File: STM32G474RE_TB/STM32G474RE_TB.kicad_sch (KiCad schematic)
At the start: 2 parts, among them U1 STM32G474RETx, Y1 ABM8G-24.000MHZ-18-D2Y-T

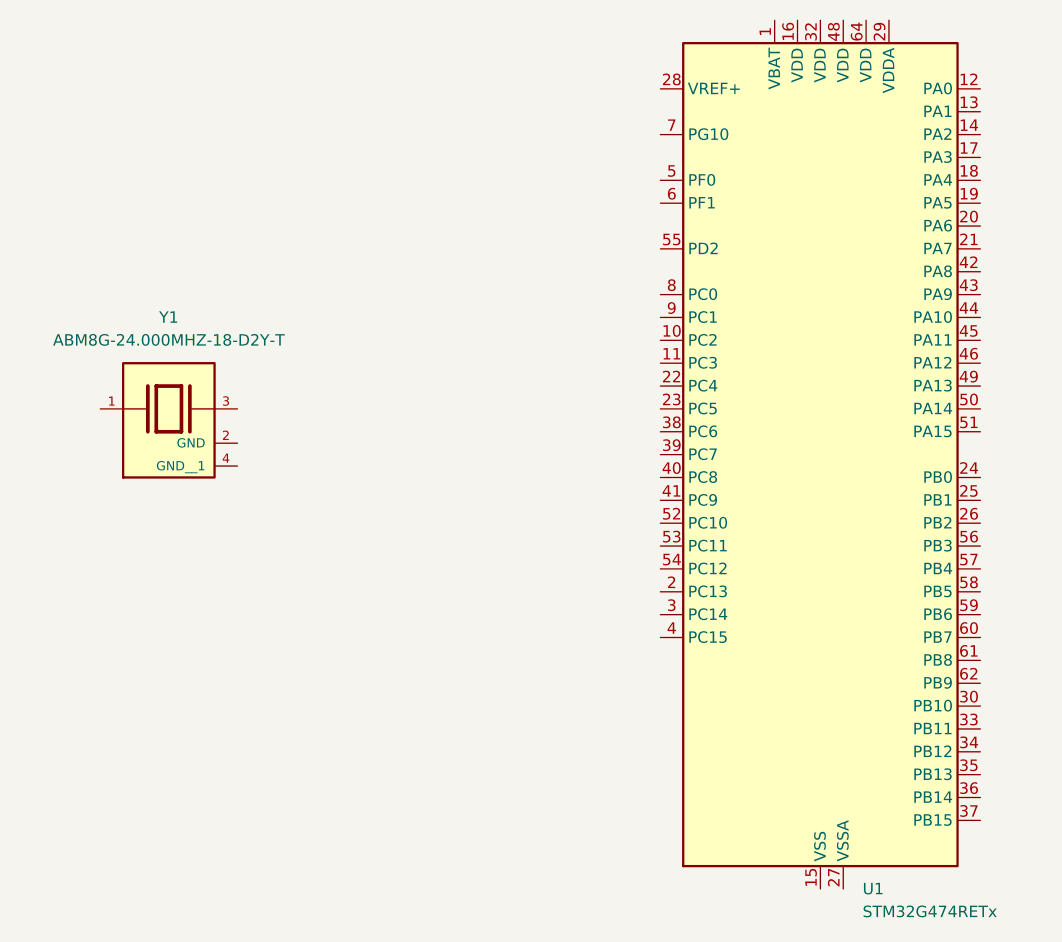
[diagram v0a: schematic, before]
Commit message: Rotated STM32 and adjusted xosc capacitor values.
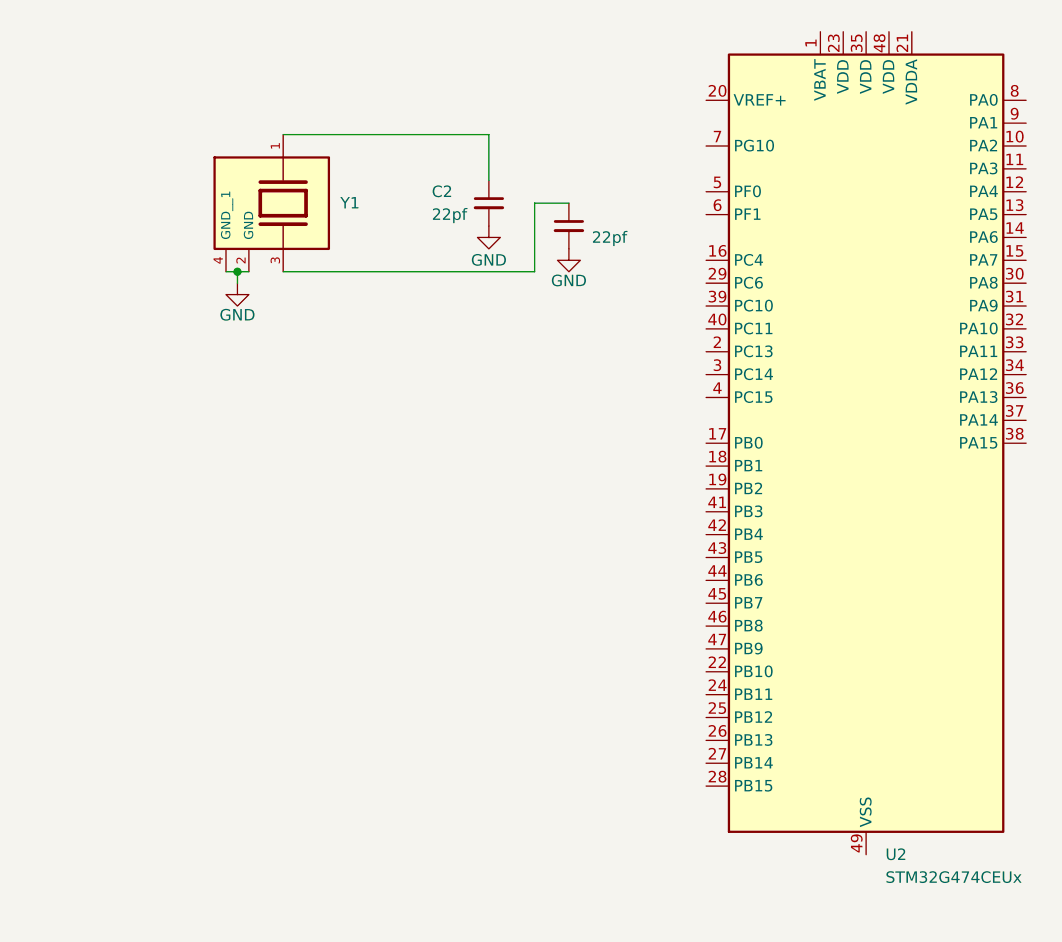
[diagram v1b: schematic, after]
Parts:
- removed U1: STM32G474RETx, Package_QFP:LQFP-64_10x10mm_P0.5mm, symbol MCU_ST_STM32G4:STM32G474RETx
- added C1, C2: 22pf, Capacitor_SMD:C_0603_1608Metric, symbol Device:C_Small
- added U2: STM32G474CEUx, Package_DFN_QFN:QFN-48-1EP_7x7mm_P0.5mm_EP5.6x5.6mm, symbol MCU_ST_STM32G4:STM32G474CEUx
- Y1: footprint ABM8G_24_000MHZ_18_D2Y_T:XTAL_ABM8G-24.000MHZ-18-D2Y-T -> Crystal:Crystal_SMD_Abracon_ABM8G-4Pin_3.2x2.5mm
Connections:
- net at Y1.1: now also C2.1
- net GND: now reaches Y1.2 (GND)
- net GND: now also Y1.4 (GND__1), C1.2, C2.2
- net at Y1.3: now also C1.1
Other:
- moved on the sheet: Y1

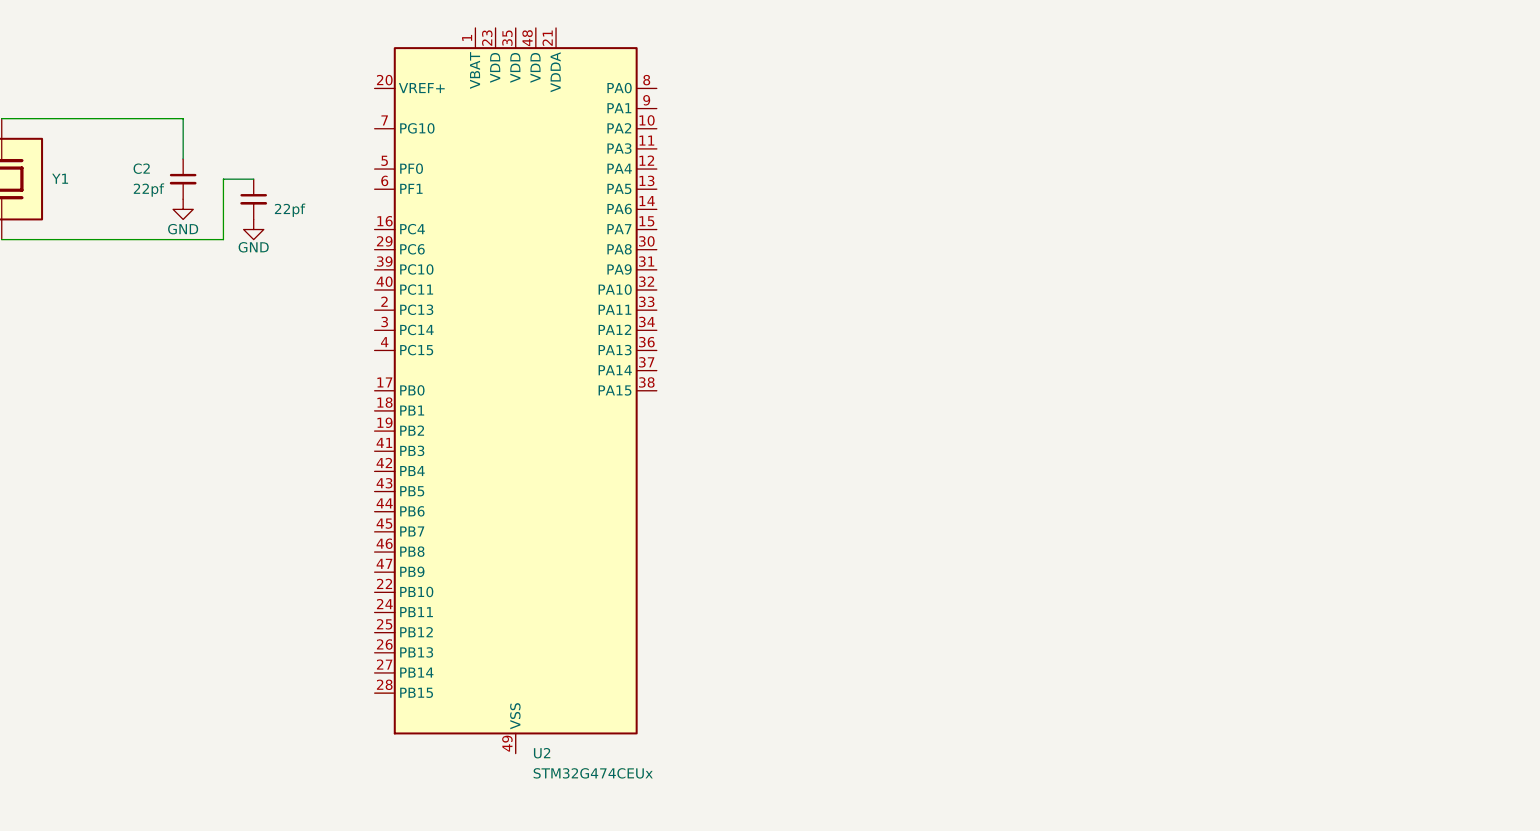
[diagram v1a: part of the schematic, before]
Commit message: Added temporary STM32Cubeide project for pin config.
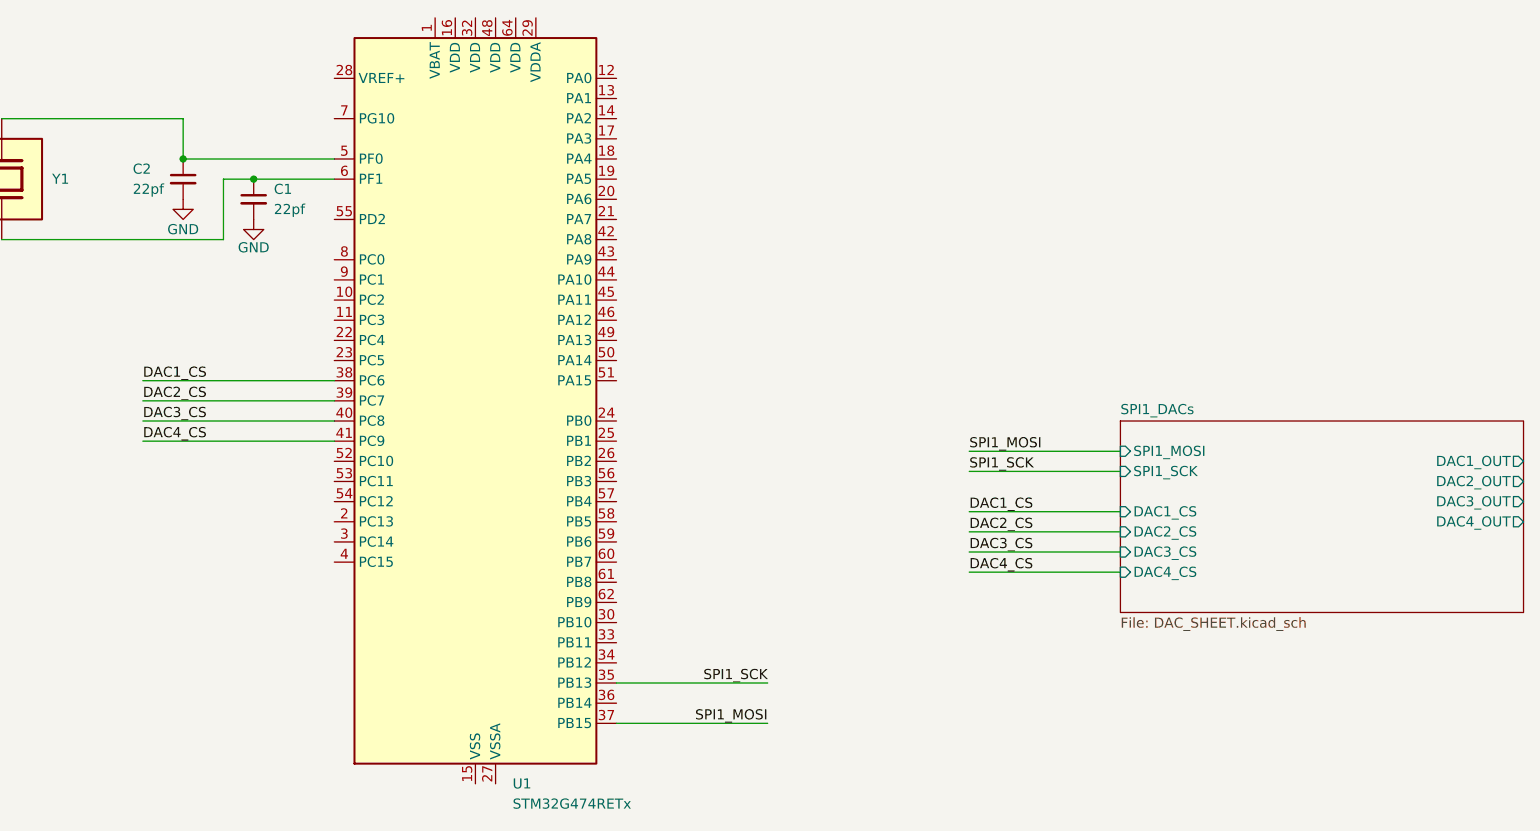
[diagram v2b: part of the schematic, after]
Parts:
- removed U2: STM32G474CEUx, Package_DFN_QFN:QFN-48-1EP_7x7mm_P0.5mm_EP5.6x5.6mm, symbol MCU_ST_STM32G4:STM32G474CEUx
- added U1: STM32G474RETx, Package_QFP:LQFP-64_10x10mm_P0.5mm, symbol MCU_ST_STM32G4:STM32G474RETx
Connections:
- net at C2.1, Y1.1: now also U1.5 (PF0)
- net at C1.1, Y1.3: now also U1.6 (PF1)
- new net: U1.15 (VSS), U1.31 (VSS), U1.47 (VSS), U1.63 (VSS)
- new net DAC1_CS: U1.38 (PC6)
- new net DAC2_CS: U1.39 (PC7)
- new net DAC3_CS: U1.40 (PC8)
- new net DAC4_CS: U1.41 (PC9)
- new net SPI1_MOSI: U1.37 (PB15)
- new net SPI1_SCK: U1.35 (PB13)
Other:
- added sheet SPI1_DACs (DAC_SHEET.kicad_sch)

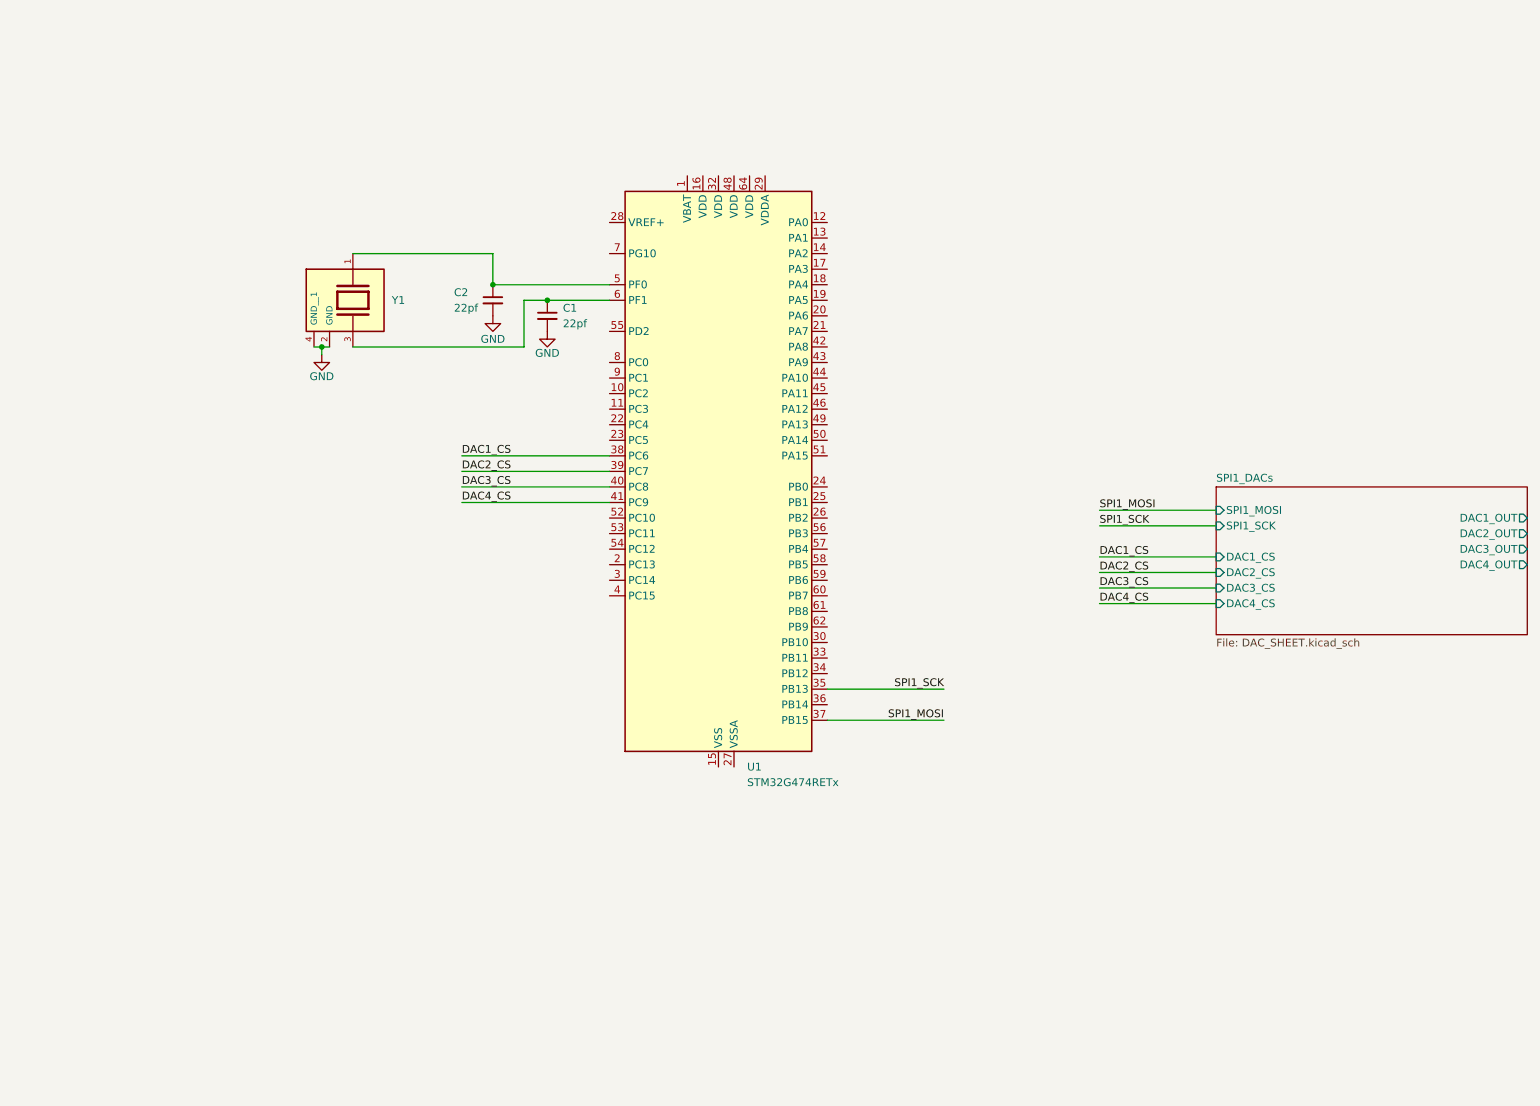
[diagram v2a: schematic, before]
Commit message: Added power LDO and built DAC buffer circuits Added pin descriptions
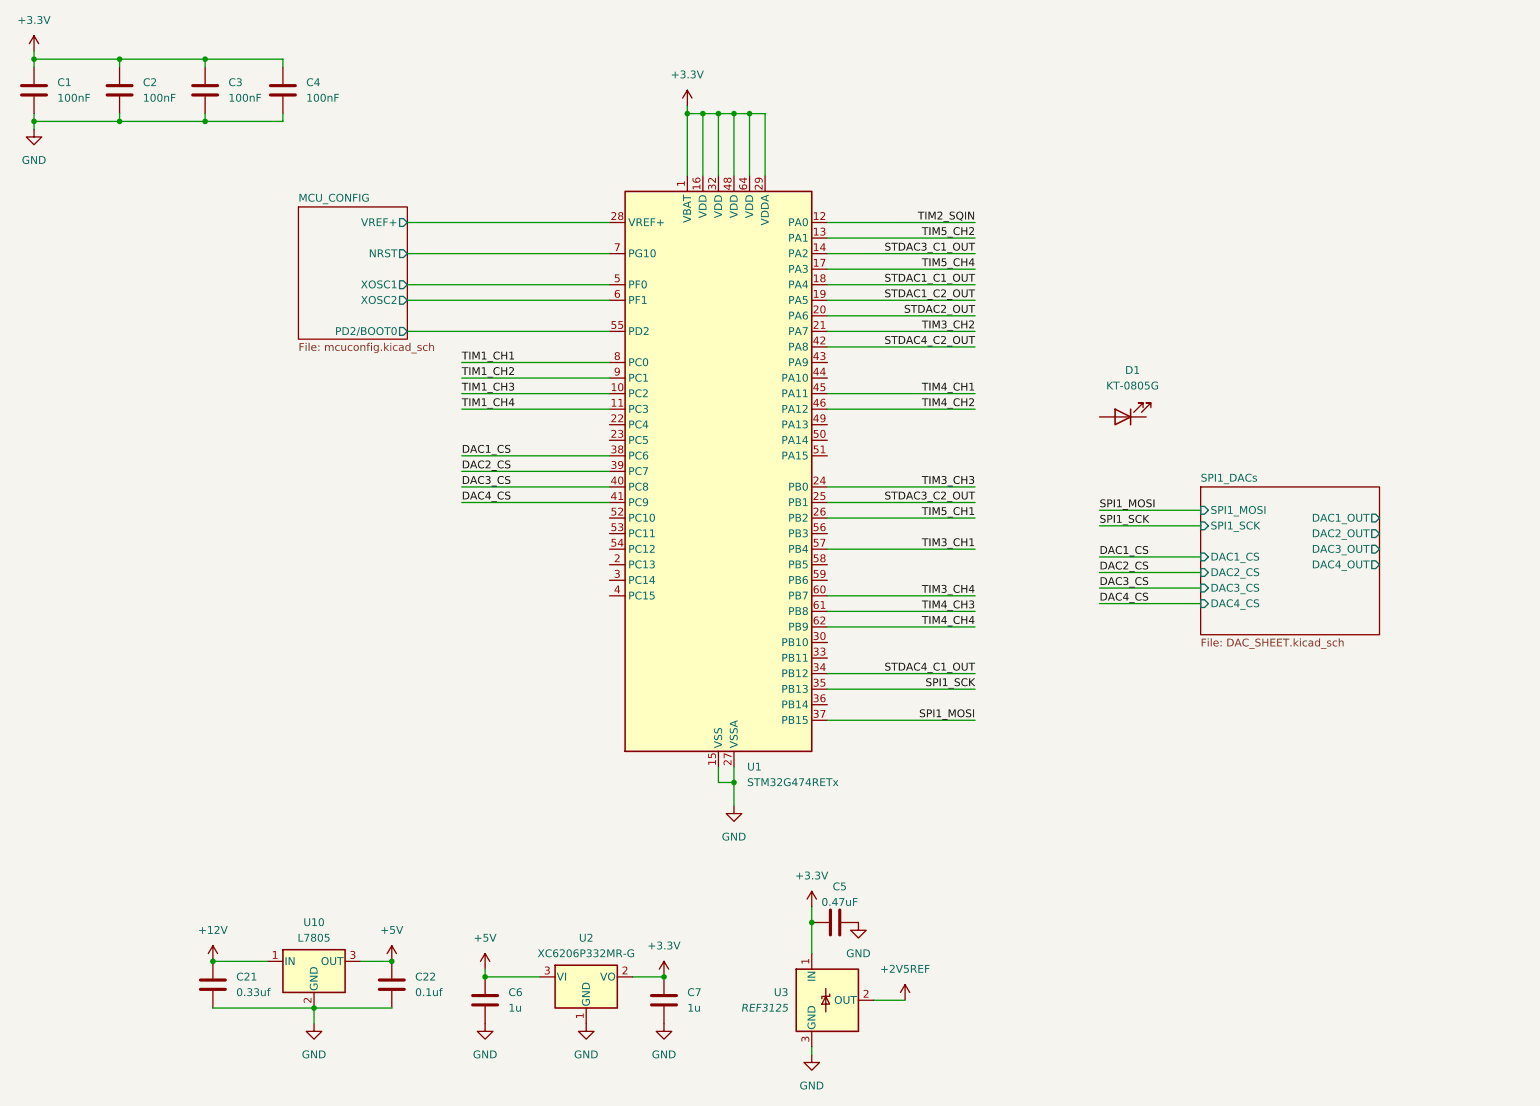
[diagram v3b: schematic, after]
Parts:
- removed C1, C2: 22pf, Capacitor_SMD:C_0603_1608Metric, symbol Device:C_Small
- removed Y1: ABM8G-24.000MHZ-18-D2Y-T, Crystal:Crystal_SMD_Abracon_ABM8G-4Pin_3.2x2.5mm, symbol ABM8G-24.000MHZ-18-D2Y-T:ABM8G-24.000MHZ-18-D2Y-T
- added C1, C2, C3, C4: 100nF, Capacitor_SMD:C_0603_1608Metric, symbol Device:C
- added C21: 0.33uf, Capacitor_SMD:C_0603_1608Metric, symbol Device:C
- added C22: 0.1uf, Capacitor_SMD:C_0603_1608Metric, symbol Device:C
- added C5: 0.47uF, Capacitor_SMD:C_0603_1608Metric, symbol Device:C
- added C6, C7: 1u, Capacitor_SMD:C_0603_1608Metric, symbol Device:C
- added D1: KT-0805G, LED_SMD:LED_0805_2012Metric, symbol Device:LED
- added U10: L7805, Package_TO_SOT_SMD:TO-252-2, symbol Regulator_Linear:L7805
- added U2: XC6206P332MR-G, Package_TO_SOT_SMD:SOT-23-3, symbol Regulator_Linear:XC6206PxxxMR
- added U3: REF3125, Package_TO_SOT_SMD:SOT-23, symbol Reference_Voltage:REF3025
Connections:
- net GND: now also U1.15 (VSS), U1.27 (VSSA), U1.31 (VSS), U1.47 (VSS), U1.63 (VSS), C1.1, C2.1, C21.1, C22.1, C3.1, C4.1, C5.2, C6.1, C7.1, U10.2 (GND), U2.1 (GND), U3.3 (GND)
- net MCU_CONFIG/XOSC1: now reaches U1.5 (PF0)
- net MCU_CONFIG/XOSC2: now reaches U1.6 (PF1)
- net +3.3V: now reaches U1.1 (VBAT)
- net +3.3V: now also U1.16 (VDD), U1.29 (VDDA), U1.32 (VDD), U1.48 (VDD), U1.64 (VDD), C1.2, C2.2, C3.2, C4.2, C5.1, C7.2, U2.2 (VO), U3.1 (IN)
- net TIM1_CH3: now reaches U1.10 (PC2)
- net TIM1_CH4: now reaches U1.11 (PC3)
- net TIM2_SQIN: now reaches U1.12 (PA0)
- net TIM5_CH2: now reaches U1.13 (PA1)
- net STDAC3_C1_OUT: now reaches U1.14 (PA2)
- net TIM5_CH4: now reaches U1.17 (PA3)
- net STDAC1_C1_OUT: now reaches U1.18 (PA4)
- net STDAC1_C2_OUT: now reaches U1.19 (PA5)
- net STDAC2_OUT: now reaches U1.20 (PA6)
- net TIM3_CH2: now reaches U1.21 (PA7)
- net TIM3_CH3: now reaches U1.24 (PB0)
- net STDAC3_C2_OUT: now reaches U1.25 (PB1)
- net TIM5_CH1: now reaches U1.26 (PB2)
- net MCU_CONFIG/VREF+: now reaches U1.28 (VREF+)
- net STDAC4_C1_OUT: now reaches U1.34 (PB12)
- net STDAC4_C2_OUT: now reaches U1.42 (PA8)
- net TIM4_CH1: now reaches U1.45 (PA11)
- net TIM4_CH2: now reaches U1.46 (PA12)
- net MCU_CONFIG/PD2/BOOT0: now reaches U1.55 (PD2)
- net TIM3_CH1: now reaches U1.57 (PB4)
- net TIM3_CH4: now reaches U1.60 (PB7)
- net TIM4_CH3: now reaches U1.61 (PB8)
- net TIM4_CH4: now reaches U1.62 (PB9)
- net MCU_CONFIG/NRST: now reaches U1.7 (PG10)
- net TIM1_CH1: now reaches U1.8 (PC0)
- net TIM1_CH2: now reaches U1.9 (PC1)
- new net +12V: C21.2, U10.1 (IN)
- new net +2V5REF: U3.2 (OUT)
- new net +5V: C22.2, C6.2, U10.3 (OUT), U2.3 (VI)
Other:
- added sheet MCU_CONFIG (mcuconfig.kicad_sch)
